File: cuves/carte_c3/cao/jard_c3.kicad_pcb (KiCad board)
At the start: 2 copper layers, 57 x 42 mm, 24 parts, among them J1 Connecteur, J2 LEDs, Q1 BPC_IPP034N03L, U1 ESP32-C3_SUPERMINI_TH, U2 BPC_Alim3_3V, X1 Trou, X2 Trou

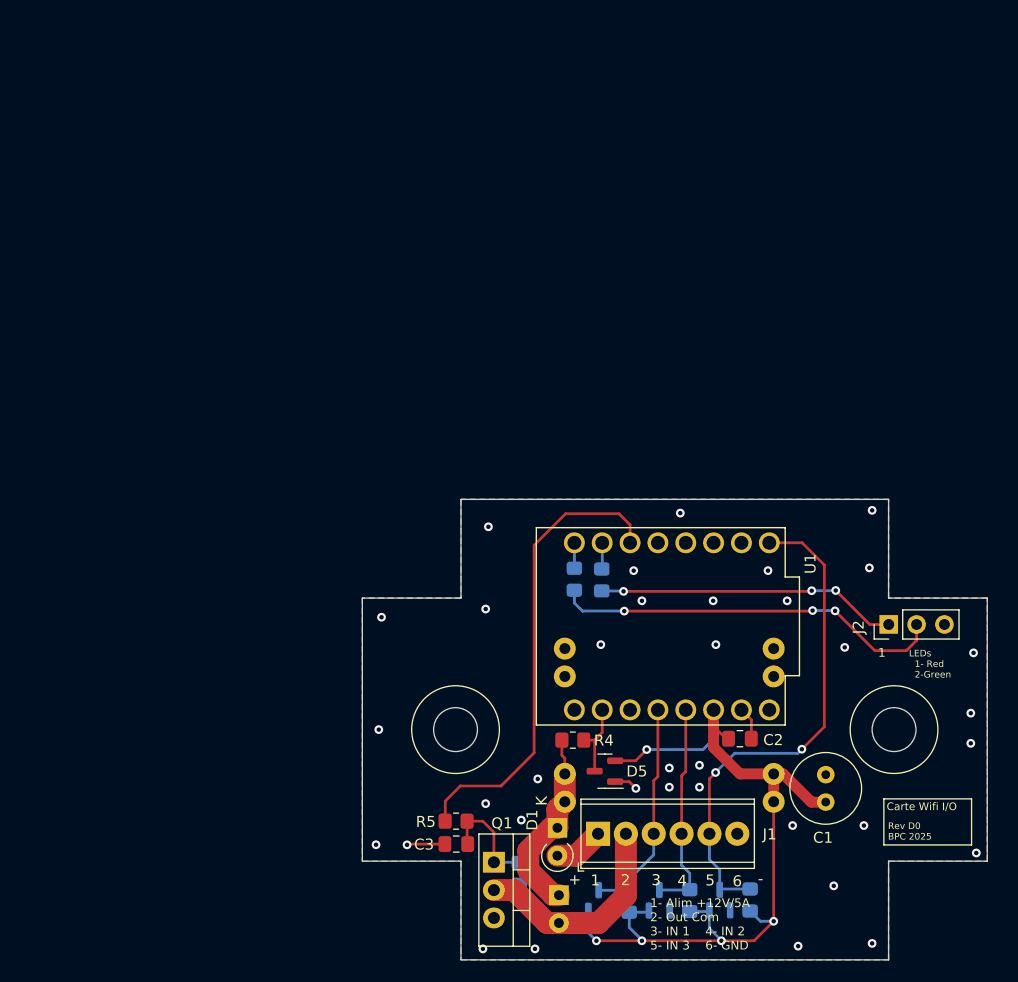
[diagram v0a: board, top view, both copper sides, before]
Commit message: Changement de la forme de la carte: Boîte 85 x 85 x 55
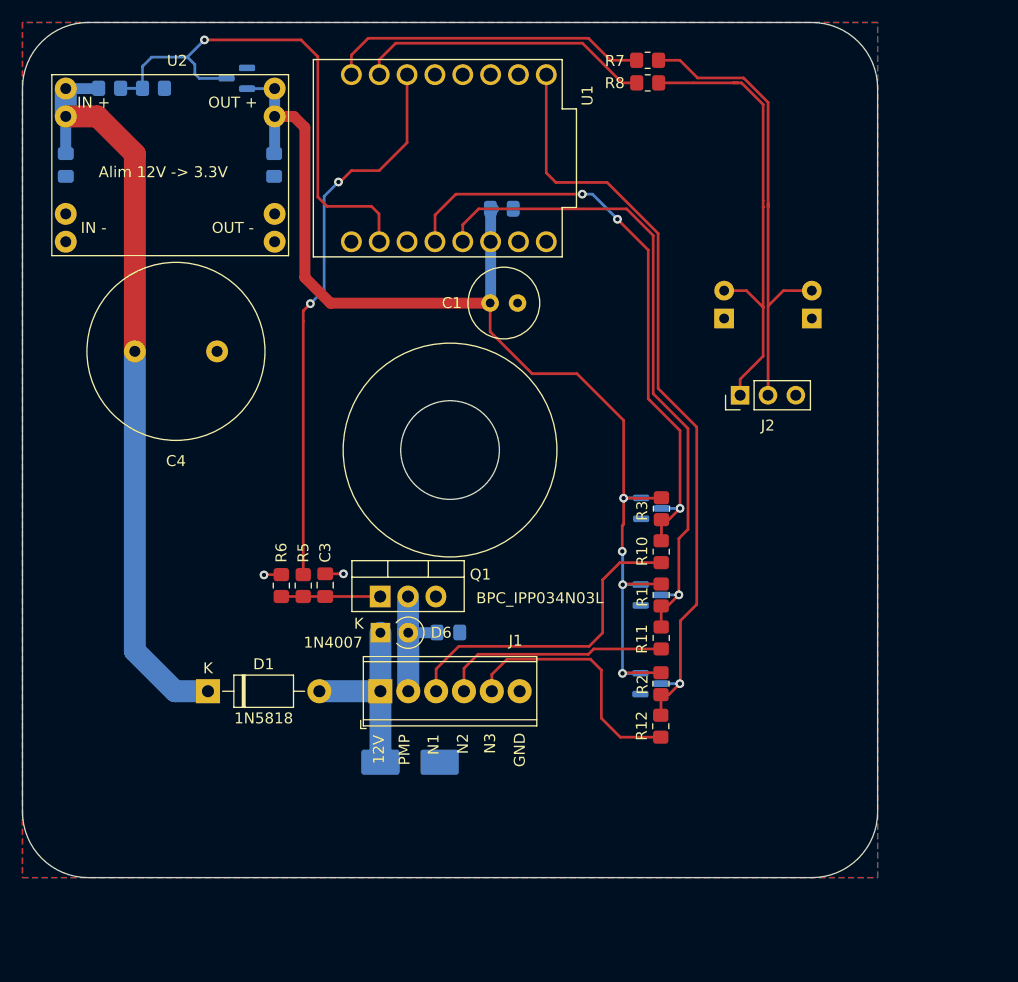
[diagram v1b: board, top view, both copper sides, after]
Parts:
- removed X1, X2: Trou, bpc:BPC_Trou4mm_Fixation
- added C4: 1000µF, Capacitor_THT:C_Radial_D16.0mm_H25.0mm_P7.50mm, F.Cu at (101.2, 75.0)
- added C5: 100n, Capacitor_SMD:C_0805_2012Metric_Pad1.18x1.45mm_HandSolder, B.Cu at (95.0, 58.0)
- added C6: 100n, Capacitor_SMD:C_0805_2012Metric_Pad1.18x1.45mm_HandSolder, B.Cu at (129.8, 100.6)
- added C7: 100n, Capacitor_SMD:C_0805_2012Metric_Pad1.18x1.45mm_HandSolder, B.Cu at (114.0, 58.0)
- added D7: SMBJ18A, Diode_SMD:D_SMB_Handsoldering, B.Cu at (126.3, 112.5)
- added D8: LED ROUGE, LED_THT:LED_D3.0mm, B.Cu at (155.0, 72.0)
- added D9: LED VERTE, LED_THT:LED_D3.0mm, B.Cu at (163.0, 72.0)
- added R10: 1k, Resistor_SMD:R_0805_2012Metric_Pad1.20x1.40mm_HandSolder, F.Cu at (149.3, 93.3)
- added R11: 1k, Resistor_SMD:R_0805_2012Metric_Pad1.20x1.40mm_HandSolder, F.Cu at (149.3, 101.1)
- added R12: 1k, Resistor_SMD:R_0805_2012Metric_Pad1.20x1.40mm_HandSolder, F.Cu at (149.2, 109.2)
- added R9: 10k, Resistor_SMD:R_0805_2012Metric_Pad1.20x1.40mm_HandSolder, B.Cu at (103.0, 51.0)
- C2, D5: moved to B.Cu
- D1: value D -> 1N5818; footprint Diode_THT:D_A-405_P2.54mm_Vertical_KathodeUp -> Diode_THT:D_DO-41_SOD81_P10.16mm_Horizontal
- D6: value D -> 1N4007; moved to F.Cu
- R1, R2, R3, R6, R7, R8, U2: moved to F.Cu
- R4: value 1,2M -> 33k; moved to B.Cu
- moved U2 79.4 mm to (95.0, 51.0)
- moved R4 72.9 mm to (99.0, 51.0)
- moved D5 71.6 mm to (110.5, 50.1)
- moved C1 54.9 mm to (133.7, 70.6), turned to 0 degrees
- moved C2 53.0 mm to (134.7, 62.0)
- moved R7 47.8 mm to (148.0, 48.5), turned to 180 degrees
- moved U1 47.3 mm to (128.9, 57.4)
- moved R8 45.5 mm to (148.0, 50.5), turned to 180 degrees
- moved D4 36.1 mm to (148.4, 89.3), turned to 0 degrees
- moved R3 35.9 mm to (149.3, 89.3), turned to -90 degrees
- moved D1 34.2 mm to (107.9, 106.0), turned to 0 degrees
- moved R6 34.1 mm to (114.6, 96.4), turned to 90 degrees
- moved D6 29.0 mm to (123.7, 100.7), turned to 0 degrees
- moved R1 28.0 mm to (149.3, 97.2), turned to 90 degrees
- moved D3 27.9 mm to (148.3, 97.2), turned to 0 degrees
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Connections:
- D1 pad 1: +12V -> Net-(D1-K)
- D1 pad 2: Net-(D1-A) -> +12V
- J1 pad 1: Net-(D1-A) -> +12V
- J1 pad 3: IN_1 -> Net-(J1-Pin_3)
- J1 pad 4: IN_2 -> Net-(J1-Pin_4)
- J1 pad 5: IN_3 -> Net-(J1-Pin_5)
- R4 pad 2: +12V -> Net-(D1-K)
- U2 pad 1: +12V -> Net-(D1-K)
- U2 pad 2: +12V -> Net-(D1-K)
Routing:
- net Net-(D1-K): track 0.00 -> 70.2 mm
- net POW_MES: track 6.87 -> 48.1 mm, vias 0 -> 1
- net IN_2: track 19.7 -> 60.5 mm, vias 0 -> 1
- net IN_1: track 20.3 -> 55.3 mm, vias 0 -> 3
- net +3V3: track 76.1 -> 108.6 mm, vias 5 -> 4
- net Net-(J1-Pin_3): track 0.00 -> 29.4 mm
- net LED_VERTE: track 2.32 -> 29.3 mm
- net LED_ROUGE: track 2.41 -> 27.0 mm
- net IN_3: track 46.4 -> 70.4 mm, vias 2 -> 1
- net Net-(J1-Pin_5): track 0.00 -> 23.0 mm
- net Net-(J1-Pin_4): track 0.00 -> 20.8 mm
- net Net-(D8-A): track 27.5 -> 42.4 mm, vias 3 -> 0
- net OUT_12V_COM: track 20.0 -> 11.3 mm
- net CMD_OUT_12V: track 42.7 -> 51.1 mm, vias 0 -> 2
- net Net-(D9-A): track 36.1 -> 43.3 mm, vias 3 -> 0
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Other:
- board size 57 x 42 mm -> 78 x 78 mm
- board text added: "12V"
- board text added: "GND"
- board text added: "N1"
- board text added: "N2"
- board text added: "N3"
- board text added: "PMP"
- board text added: "ROUGE"
- board text added: "VERT"
- board text removed: "+"
- board text removed: "-"
- board text removed: "1"
- board text removed: "1- Alim +12V/5A 2- Out Com 3- IN 1 4- IN 2 5- IN 3 6- GND"
- board text removed: "2"
- board text removed: "3"
- board text removed: "4"
- board text removed: "5"
- board text removed: "6"
- board text removed: "Carte Wifi I/O"
- board text removed: "LEDs 1- Red 2-Green"
- board text removed: "Rev D0 BPC 2025"

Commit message: Finalisation / règles kicad...
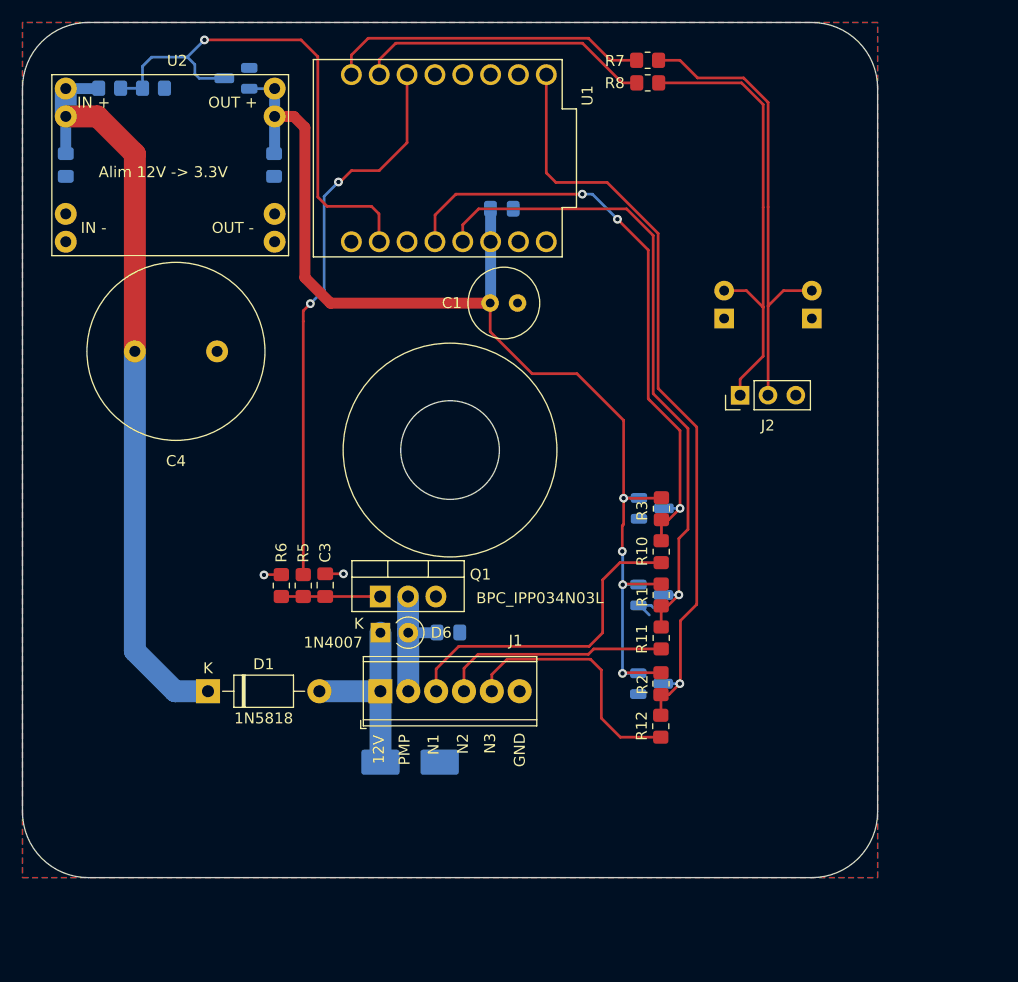
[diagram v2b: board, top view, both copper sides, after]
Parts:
- D2, D3, D4, D5: footprint Package_TO_SOT_SMD:SOT-23 -> bpc:BPC_SOT-23-3_HandSoldering
- R4: value 33k -> 39k
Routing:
- net GND: track 3.26 -> 6.15 mm
